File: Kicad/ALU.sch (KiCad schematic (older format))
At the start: 10 parts, among them U17 74HCT153, U18 74HCT153, U19 74HCT153, U20 74HCT153, U21 74HCT153, U22 74HCT153, U23 74HCT153, U24 74HCT153, U25 74HCT283, U26 74HCT283

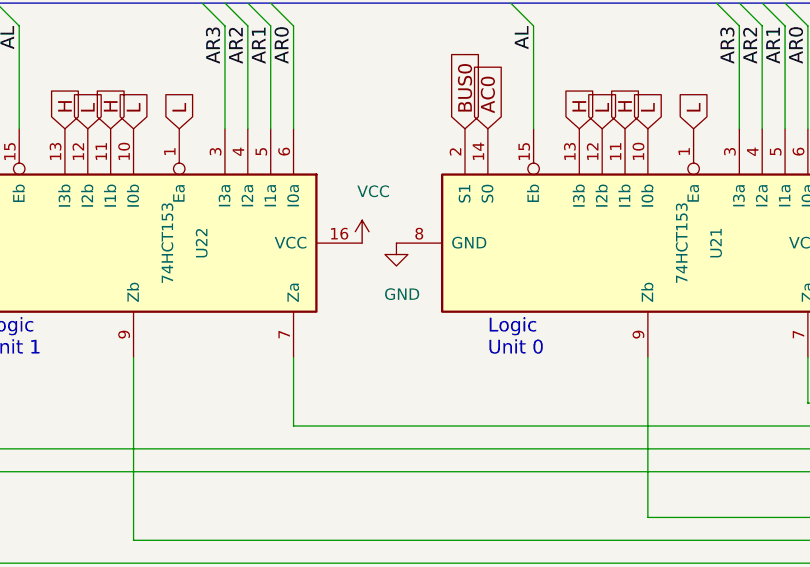
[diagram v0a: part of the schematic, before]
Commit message: Update to work with mostly the default KiCAD items or items downloaded via the KiCAD Libraries too.
2 Resistors added of 1k on the lines for TRUE and FALSE pull ups.

Several things deleted which appeared at Graphic shapes on the PCB sometimes
but could not be edited. this was done manually at the bottom of the PCB_KiCAD file.

Deleted some PCB items around the order which marked the Copper limits of top and bottom. may have been tied to TRUE & FALSE.

Changed USB socket type.

This has been done not to change the board but to aid understanding and allow anyone who wants slightly easier access.

I have not tested it and provide no warranty.

Signed-off-by: John Bradley <flypie@rocketmail.com>
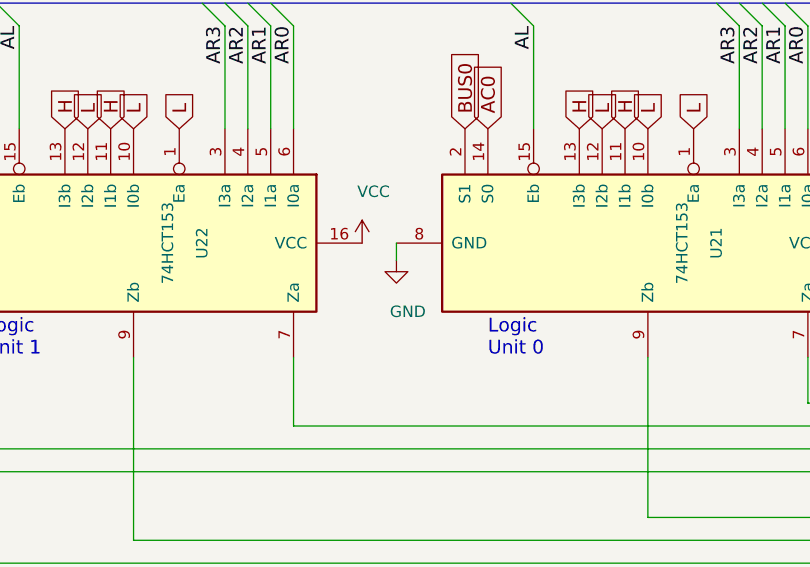
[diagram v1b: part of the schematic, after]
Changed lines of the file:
@@
 	9600 3450 9600 3825
 $Comp
-L power:GND #PWR?
+L power:GND #PWR0133
 U 1 1 5FAE774C
 P 950 1575
-F 0 "#PWR?" H 950 1325 50  0001 C CNN
+F 0 "#PWR0133" H 950 1325 50  0001 C CNN
 F 1 "GND" H 975 1350 50  0000 C CNN
 F 2 "" H 950 1575 50  0001 C CNN
@@
 $EndComp
 $Comp
-L power:VCC #PWR?
+L power:VCC #PWR0134
 U 1 1 5FAE7AC0
 P 3050 1575
-F 0 "#PWR?" H 3050 1425 50  0001 C CNN
+F 0 "#PWR0134" H 3050 1425 50  0001 C CNN
 F 1 "VCC" H 3100 1800 50  0000 C CNN
 F 2 "" H 3050 1575 50  0001 C CNN
@@
 $EndComp
 $Comp
-L power:GND #PWR?
+L power:GND #PWR0135
 U 1 1 5FAEADF0
 P 3200 1575
-F 0 "#PWR?" H 3200 1325 50  0001 C CNN
+F 0 "#PWR0135" H 3200 1325 50  0001 C CNN
 F 1 "GND" H 3225 1350 50  0000 C CNN
 F 2 "" H 3200 1575 50  0001 C CNN
@@
 $EndComp
 $Comp
-L power:VCC #PWR?
+L power:VCC #PWR0136
 U 1 1 5FAEADFA
 P 5300 1575
-F 0 "#PWR?" H 5300 1425 50  0001 C CNN
+F 0 "#PWR0136" H 5300 1425 50  0001 C CNN
 F 1 "VCC" H 5350 1800 50  0000 C CNN
 F 2 "" H 5300 1575 50  0001 C CNN
@@
 $EndComp
 $Comp
-L power:GND #PWR?
+L power:GND #PWR0137
 U 1 1 5FAF0C0A
 P 5450 1575
-F 0 "#PWR?" H 5450 1325 50  0001 C CNN
+F 0 "#PWR0137" H 5450 1325 50  0001 C CNN
 F 1 "GND" H 5475 1350 50  0000 C CNN
 F 2 "" H 5450 1575 50  0001 C CNN
@@
 $EndComp
 $Comp
-L power:VCC #PWR?
+L power:VCC #PWR0138
 U 1 1 5FAF0C14
 P 7550 1575
-F 0 "#PWR?" H 7550 1425 50  0001 C CNN
+F 0 "#PWR0138" H 7550 1425 50  0001 C CNN
 F 1 "VCC" H 7600 1800 50  0000 C CNN
 F 2 "" H 7550 1575 50  0001 C CNN
@@
 $EndComp
 $Comp
-L power:GND #PWR?
+L power:GND #PWR0139
 U 1 1 5FAF0C1E
-P 7700 1575
-F 0 "#PWR?" H 7700 1325 50  0001 C CNN
-F 1 "GND" H 7725 1350 50  0000 C CNN
-F 2 "" H 7700 1575 50  0001 C CNN
-F 3 "" H 7700 1575 50  0001 C CNN
-	1    7700 1575
-	1    0    0    -1
-$EndComp
-$Comp
-L power:VCC #PWR?
+P 7700 1650
+F 0 "#PWR0139" H 7700 1400 50  0001 C CNN
+F 1 "GND" H 7750 1425 50  0000 C CNN
+F 2 "" H 7700 1650 50  0001 C CNN
+F 3 "" H 7700 1650 50  0001 C CNN
+	1    7700 1650
+	1    0    0    -1
+$EndComp
+$Comp
+L power:VCC #PWR0140
 U 1 1 5FAF0C28
 P 9800 1575
-F 0 "#PWR?" H 9800 1425 50  0001 C CNN
+F 0 "#PWR0140" H 9800 1425 50  0001 C CNN
 F 1 "VCC" H 9850 1800 50  0000 C CNN
 F 2 "" H 9800 1575 50  0001 C CNN
@@
 $EndComp
 $Comp
-L power:VCC #PWR?
+L power:VCC #PWR0141
 U 1 1 5FAF4200
 P 10100 1775
-F 0 "#PWR?" H 10100 1625 50  0001 C CNN
+F 0 "#PWR0141" H 10100 1625 50  0001 C CNN
 F 1 "VCC" V 10100 1925 50  0000 L CNN
 F 2 "" H 10100 1775 50  0001 C CNN
@@
 $EndComp
 $Comp
-L power:GND #PWR?
+L power:GND #PWR0142
 U 1 1 5FAF9B92
 P 3050 5325
-F 0 "#PWR?" H 3050 5075 50  0001 C CNN
+F 0 "#PWR0142" H 3050 5075 50  0001 C CNN
 F 1 "GND" H 3075 5100 50  0000 C CNN
 F 2 "" H 3050 5325 50  0001 C CNN
@@
 $EndComp
 $Comp
-L power:VCC #PWR?
+L power:VCC #PWR0143
 U 1 1 5FAF9B9C
 P 950 5325
-F 0 "#PWR?" H 950 5175 50  0001 C CNN
+F 0 "#PWR0143" H 950 5175 50  0001 C CNN
 F 1 "VCC" H 1000 5550 50  0000 C CNN
 F 2 "" H 950 5325 50  0001 C CNN
@@
 $EndComp
 $Comp
-L power:GND #PWR?
+L power:GND #PWR0144
 U 1 1 5FAF9BA6
 P 5300 5325
-F 0 "#PWR?" H 5300 5075 50  0001 C CNN
+F 0 "#PWR0144" H 5300 5075 50  0001 C CNN
 F 1 "GND" H 5325 5100 50  0000 C CNN
 F 2 "" H 5300 5325 50  0001 C CNN
@@
 $EndComp
 $Comp
-L power:VCC #PWR?
+L power:VCC #PWR0145
 U 1 1 5FAF9BB0
 P 3200 5325
-F 0 "#PWR?" H 3200 5175 50  0001 C CNN
+F 0 "#PWR0145" H 3200 5175 50  0001 C CNN
 F 1 "VCC" H 3250 5550 50  0000 C CNN
 F 2 "" H 3200 5325 50  0001 C CNN
@@
 $EndComp
 $Comp
-L power:GND #PWR?
+L power:GND #PWR0146
 U 1 1 5FAF9BBA
 P 7550 5325
-F 0 "#PWR?" H 7550 5075 50  0001 C CNN
+F 0 "#PWR0146" H 7550 5075 50  0001 C CNN
 F 1 "GND" H 7575 5100 50  0000 C CNN
 F 2 "" H 7550 5325 50  0001 C CNN
@@
 $EndComp
 $Comp
-L power:VCC #PWR?
+L power:VCC #PWR0147
 U 1 1 5FAF9BC4
 P 5450 5325
-F 0 "#PWR?" H 5450 5175 50  0001 C CNN
+F 0 "#PWR0147" H 5450 5175 50  0001 C CNN
 F 1 "VCC" H 5500 5550 50  0000 C CNN
 F 2 "" H 5450 5325 50  0001 C CNN
@@
 $EndComp
 $Comp
-L power:GND #PWR?
+L power:GND #PWR0148
 U 1 1 5FAF9BCE
 P 9800 5325
-F 0 "#PWR?" H 9800 5075 50  0001 C CNN
+F 0 "#PWR0148" H 9800 5075 50  0001 C CNN
 F 1 "GND" H 9825 5100 50  0000 C CNN
 F 2 "" H 9800 5325 50  0001 C CNN
@@
 $EndComp
 $Comp
-L power:VCC #PWR?
+L power:VCC #PWR0149
 U 1 1 5FAF9BD8
 P 7700 5325
-F 0 "#PWR?" H 7700 5175 50  0001 C CNN
+F 0 "#PWR0149" H 7700 5175 50  0001 C CNN
 F 1 "VCC" H 7750 5550 50  0000 C CNN
 F 2 "" H 7700 5325 50  0001 C CNN
@@
 $EndComp
 $Comp
-L power:GND #PWR?
+L power:GND #PWR0150
 U 1 1 5FAF9C0A
 P 10100 3375
-F 0 "#PWR?" H 10100 3125 50  0001 C CNN
+F 0 "#PWR0150" H 10100 3125 50  0001 C CNN
 F 1 "GND" V 10150 3225 50  0000 R CNN
 F 2 "" H 10100 3375 50  0001 C CNN
@@
 $EndComp
 $Comp
-L power:GND #PWR?
+L power:GND #PWR0151
 U 1 1 5FAF9C1E
 P 10100 5125
-F 0 "#PWR?" H 10100 4875 50  0001 C CNN
+F 0 "#PWR0151" H 10100 4875 50  0001 C CNN
 F 1 "GND" H 10125 4900 50  0000 C CNN
 F 2 "" H 10100 5125 50  0001 C CNN
@@
 $EndComp
 $Comp
-L power:VCC #PWR?
+L power:VCC #PWR0152
 U 1 1 5FAF9C28
 P 10100 3525
-F 0 "#PWR?" H 10100 3375 50  0001 C CNN
+F 0 "#PWR0152" H 10100 3375 50  0001 C CNN
 F 1 "VCC" V 10100 3700 50  0000 L CNN
 F 2 "" H 10100 3525 50  0001 C CNN
@@
 	0    1    1    0
 $EndComp
+Wire Wire Line
+	7700 1650 7700 1575
 Wire Bus Line
 	500  625  500  6325
